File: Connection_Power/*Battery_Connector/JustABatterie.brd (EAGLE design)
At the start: 20 x 13 mm, 2 parts

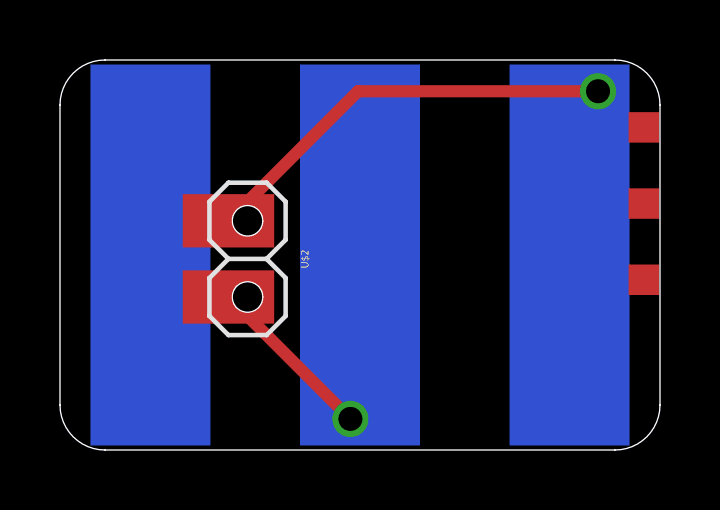
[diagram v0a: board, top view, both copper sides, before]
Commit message: Update Pinheader
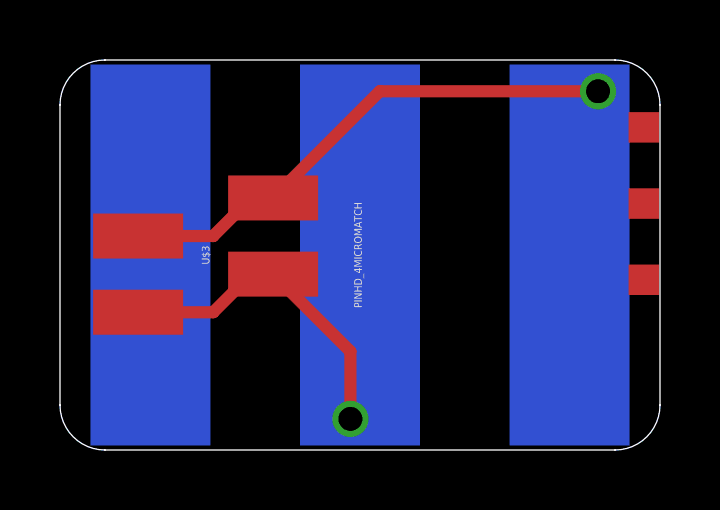
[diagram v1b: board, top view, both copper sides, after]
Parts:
- removed U$2: PINHD_22.54MOD, thar:PINHD_2_MOD
- added U$3: PINHD_4MICROMATCH, thar:MICROMATCH4P0L
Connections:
- net N$2: now also U$3.P$3, U$3.P$4; no longer U$2.P$1
- net N$3: now also U$3.P$1, U$3.P$2; no longer U$2.P$2
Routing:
- net N$3: track 11.3 -> 16.5 mm
- net N$2: track 25.5 -> 28.7 mm
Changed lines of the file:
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@@
 <layer number="56" name="wert" color="7" fill="1" visible="no" active="no"/>
 <layer number="57" name="tCAD" color="7" fill="1" visible="no" active="no"/>
+<layer number="90" name="Modules" color="5" fill="1" visible="no" active="no"/>
 <layer number="91" name="Nets" color="2" fill="1" visible="no" active="no"/>
 <layer number="92" name="Busses" color="1" fill="1" visible="no" active="no"/>
@@
 <layer number="97" name="Info" color="7" fill="1" visible="no" active="no"/>
 <layer number="98" name="Guide" color="6" fill="1" visible="no" active="no"/>
+<layer number="99" name="SpiceOrder" color="7" fill="1" visible="no" active="no"/>
 <layer number="100" name="Muster" color="7" fill="1" visible="no" active="no"/>
 <layer number="101" name="Patch_Top" color="12" fill="4" visible="yes" active="yes"/>
@@
 <layer number="111" name="LPC17xx" color="7" fill="1" visible="yes" active="yes"/>
 <layer number="112" name="tSilk" color="7" fill="1" visible="yes" active="yes"/>
+<layer number="113" name="IDFDebug" color="7" fill="1" visible="yes" active="yes"/>
 <layer number="116" name="Patch_BOT" color="9" fill="4" visible="yes" active="yes"/>
 <layer number="118" name="Rect_Pads" color="7" fill="1" visible="yes" active="yes"/>
@@
 <elements>
 <element name="U$1" library="thar" package="CARRIER_SMD2_3POL" value="CARRIER_SMD2SMD2_3POL" x="11.75" y="7.75" locked="yes" rot="R180"/>
-<element name="U$2" library="thar" package="PINHD_2_MOD" value="PINHD_22.54MOD" x="8.001" y="7.62" rot="R270"/>
+<element name="U$3" library="thar" package="MICROMATCH4P0L" value="PINHD_4MICROMATCH" x="6.604" y="7.747" smashed="yes" rot="R90">
+<attribute name="NAME" x="6.604" y="7.747" size="0.254" layer="25" rot="R90" align="center"/>
+<attribute name="VALUE" x="11.684" y="7.747" size="0.254" layer="25" rot="R90" align="center"/>
+</element>
 </elements>
 <signals>
@@
 <signal name="N$2">
 <contactref element="U$1" pad="GND"/>
-<contactref element="U$2" pad="P$1"/>
 <via x="19.685" y="13.208" extent="1-16" drill="0.8" shape="octagon"/>
-<wire x1="11.684" y1="13.208" x2="19.685" y2="13.208" width="0.4064" layer="1"/>
 <wire x1="19.685" y1="13.208" x2="19.75" y2="13.208" width="0.4064" layer="16"/>
 <wire x1="19.75" y1="13.208" x2="19.75" y2="7.75" width="0.4064" layer="16"/>
-<wire x1="7.366" y1="8.89" x2="11.684" y2="13.208" width="0.4064" layer="1"/>
 <wire x1="18.735" y1="7.75" x2="18.735" y2="12.258" width="0.254" layer="16"/>
 <wire x1="18.735" y1="12.258" x2="19.685" y2="13.208" width="0.254" layer="16"/>
+<contactref element="U$3" pad="P$4"/>
+<contactref element="U$3" pad="P$3"/>
+<wire x1="19.685" y1="13.208" x2="12.41" y2="13.208" width="0.4064" layer="1"/>
+<wire x1="12.41" y1="13.208" x2="8.854" y2="9.652" width="0.4064" layer="1"/>
+<wire x1="4.354" y1="8.382" x2="6.858" y2="8.382" width="0.4064" layer="1"/>
+<wire x1="6.858" y1="8.382" x2="8.001" y2="9.525" width="0.4064" layer="1"/>
+<wire x1="8.001" y1="9.525" x2="8.727" y2="9.525" width="0.4064" layer="1"/>
+<wire x1="8.727" y1="9.525" x2="8.854" y2="9.652" width="0.4064" layer="1"/>
 </signal>
 <signal name="N$3">
 <contactref element="U$1" pad="VCC"/>
-<contactref element="U$2" pad="P$2"/>
 <via x="11.43" y="2.286" extent="1-16" drill="0.8" shape="octagon"/>
-<wire x1="7.366" y1="6.35" x2="11.43" y2="2.286" width="0.4064" layer="1"/>
 <wire x1="11.75" y1="7.75" x2="11.75" y2="2.606" width="0.254" layer="16"/>
 <wire x1="11.75" y1="2.606" x2="11.43" y2="2.286" width="0.254" layer="16"/>
+<contactref element="U$3" pad="P$1"/>
+<contactref element="U$3" pad="P$2"/>
+<wire x1="11.43" y1="2.286" x2="11.43" y2="4.536" width="0.4064" layer="1"/>
+<wire x1="11.43" y1="4.536" x2="8.854" y2="7.112" width="0.4064" layer="1"/>
+<wire x1="4.354" y1="5.842" x2="6.858" y2="5.842" width="0.4064" layer="1"/>
+<wire x1="6.858" y1="5.842" x2="8.128" y2="7.112" width="0.4064" layer="1"/>
+<wire x1="8.128" y1="7.112" x2="8.854" y2="7.112" width="0.4064" layer="1"/>
 </signal>
 </signals>
